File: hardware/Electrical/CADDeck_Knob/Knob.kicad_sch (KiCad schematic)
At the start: 8 parts, among them J1 Conn_01x01_Pin, J2 Conn_01x01_Pin, J3 Conn_01x01_Pin, J4 Conn_01x01_Pin, J5 Conn_01x01_Pin, J6 Conn_01x02_Pin, J7 Conn_01x02_Pin, U1 49E

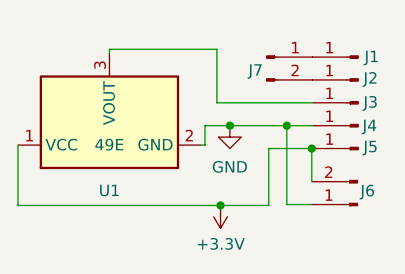
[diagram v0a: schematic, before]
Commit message: Knob Platine hatte Fehler
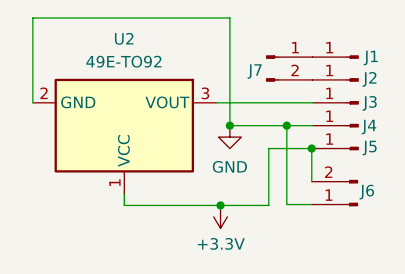
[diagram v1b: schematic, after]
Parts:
- removed U1: 49E, Package_TO_SOT_THT:TO-92S, symbol Sensor_Magnetic:A1301KUA-T
- added U2: 49E-TO92, Hallsensor 49E:49E-TO92, symbol Sensor_Magnetic:49E-TO92
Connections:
- net +3.3V: now also U2.1 (VCC)
- net GND: now also U2.2 (GND)
- net at J3.1 (Pin_1): now also U2.3 (VOUT)
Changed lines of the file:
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@@
 (kicad_sch (version 20230121) (generator eeschema)
   (paper "A4")
+  (junction (at 162.052 104.14) (diameter 0) (color 0 0 0 0)
+  )
   (junction (at 171.1452 106.68) (diameter 0) (color 0 0 0 0)
   )
-  (junction (at 162.052 104.14) (diameter 0) (color 0 0 0 0)
-  )
   (junction (at 168.3766 104.14) (diameter 0) (color 0 0 0 0)
   )
@@
     (stroke (width 0) (type default))
   )
-  (wire (pts (xy 148.6662 95.6564) (xy 160.6042 95.6564))
-    (stroke (width 0) (type default))
-  )
-  (wire (pts (xy 159.2834 106.2736) (xy 159.2834 104.1146))
-    (stroke (width 0) (type default))
-  )
-  (wire (pts (xy 159.3342 104.1146) (xy 159.3342 104.14))
-    (stroke (width 0) (type default))
-  )
-  (wire (pts (xy 148.6662 95.6564) (xy 148.6662 96.139))
-    (stroke (width 0) (type default))
-  )
-  (wire (pts (xy 138.5062 113.0046) (xy 161.0106 113.0046))
-    (stroke (width 0) (type default))
-  )
-  (wire (pts (xy 159.3342 104.14) (xy 162.052 104.14))
+  (wire (pts (xy 140.1572 101.6) (xy 140.1572 92.1766))
+    (stroke (width 0) (type default))
+  )
+  (wire (pts (xy 150.3172 113.0046) (xy 161.0106 113.0046))
+    (stroke (width 0) (type default))
+  )
+  (wire (pts (xy 150.3172 111.76) (xy 150.3172 113.0046))
     (stroke (width 0) (type default))
   )
@@
     (stroke (width 0) (type default))
   )
+  (wire (pts (xy 140.1572 92.1766) (xy 162.052 92.1766))
+    (stroke (width 0) (type default))
+  )
   (wire (pts (xy 166.37 106.68) (xy 166.37 113.0046))
     (stroke (width 0) (type default))
   )
-  (wire (pts (xy 138.5062 113.0046) (xy 138.5062 106.299))
-    (stroke (width 0) (type default))
-  )
-  (wire (pts (xy 160.6042 95.6564) (xy 160.6042 101.6))
+  (wire (pts (xy 162.052 92.1766) (xy 162.052 104.14))
     (stroke (width 0) (type default))
   )
@@
     (stroke (width 0) (type default))
   )
-  (wire (pts (xy 159.258 106.2736) (xy 159.258 106.299))
-    (stroke (width 0) (type default))
-  )
   (wire (pts (xy 161.0106 113.0046) (xy 166.37 113.0046))
     (stroke (width 0) (type default))
   )
-  (wire (pts (xy 159.258 106.2736) (xy 159.2834 106.2736))
-    (stroke (width 0) (type default))
-  )
-  (wire (pts (xy 159.258 106.299) (xy 158.8262 106.299))
-    (stroke (width 0) (type default))
-  )
   (wire (pts (xy 171.1452 106.68) (xy 171.1452 110.363))
     (stroke (width 0) (type default))
   )
   (wire (pts (xy 162.052 104.14) (xy 168.3766 104.14))
-    (stroke (width 0) (type default))
-  )
-  (wire (pts (xy 159.2834 104.1146) (xy 159.3342 104.1146))
     (stroke (width 0) (type default))
   )
@@
     )
   )
-  (symbol (lib_id "Sensor_Magnetic:A1301KUA-T") (at 148.6662 103.759 90) (unit 1)
-    (in_bom yes) (on_board yes) (dnp no)
-    (property "Reference" "U1" (at 148.6662 111.379 90)
-      (effects (font (size 1.27 1.27)))
-    )
-    (property "Value" "49E" (at 148.6662 106.299 90)
-      (effects (font (size 1.27 1.27)))
-    )
-    (property "Footprint" "Package_TO_SOT_THT:TO-92S" (at 157.5562 103.759 0)
+  (symbol (lib_id "Sensor_Magnetic:49E-TO92") (at 150.3172 104.14 270) (unit 1)
+    (in_bom yes) (on_board yes) (dnp no) (fields_autoplaced)
+    (property "Reference" "U2" (at 150.3172 94.5388 90)
+      (effects (font (size 1.27 1.27)))
+    )
+    (property "Value" "49E-TO92" (at 150.3172 97.0788 90)
+      (effects (font (size 1.27 1.27)))
+    )
+    (property "Footprint" "Hallsensor 49E:49E-TO92" (at 141.4272 104.14 0)
       (effects (font (size 1.27 1.27) italic) (justify left) hide)
     )
-    (property "Datasheet" "http://www.allegromicro.com/~/media/Files/Datasheets/A1301-2-Datasheet.ashx" (at 148.6662 106.299 0)
+    (property "Datasheet" "" (at 150.3172 101.6 0)
       (effects (font (size 1.27 1.27)) hide)
     )
@@
       (project "Knob"
         (path "/472b57b2-9bbe-4028-ab3c-fb0ce2578d6d"
-          (reference "U1") (unit 1)
-        )
-      )
+          (reference "U2") (unit 1)
+        )
+      )
